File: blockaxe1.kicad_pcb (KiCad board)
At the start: 2 copper layers, 89 parts, among them J1 TC2030-IDC, J3 Conn_01x04, J4 USB_C_Receptacle_USB2.0, J5 Conn_01x02, Q1 2N7002K, U10 DS4432U+, U11 EMC2101, U2 STM32F410CBU6, U5 MCP1824T-1802E, U6 MCP1824T-0802E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

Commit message: migrated over lots of bitaxe parts to blockaxe
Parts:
- added C45: 1uF, Capacitor_SMD:C_0402_1005Metric, F.Cu at (159.9, 132.6)
- added C46: 1uF, Capacitor_SMD:C_0402_1005Metric, F.Cu at (159.9, 134.5)
- added C47: 0.1uF, Capacitor_SMD:C_0402_1005Metric, F.Cu at (162.8, 128.6)
- added C48: 0.1uF, Capacitor_SMD:C_0402_1005Metric, F.Cu at (162.8, 130.6)
- added C49: 1uF, Capacitor_SMD:C_0402_1005Metric, F.Cu at (162.8, 132.6)
- added C50: 1uF, Capacitor_SMD:C_0402_1005Metric, F.Cu at (162.8, 134.5)
- added C51: 330uF, Capacitor_Tantalum_SMD:CP_EIA-7343-31_Kemet-D_Pad2.25x2.55mm_HandSolder, F.Cu at (162.0, 111.8)
- added C7: 0.1uF, Capacitor_SMD:C_0402_1005Metric, F.Cu at (157.1, 128.6)
- added C8: 0.1uF, Capacitor_SMD:C_0402_1005Metric, F.Cu at (157.1, 130.6)
- added J2: TC2030-IDC, blockaxe:Tag-Connect_TC2030-IDC-NL_2x03_P1.27mm_Vertical, F.Cu at (167.3, 79.8)
- added R11: 78.7k 1%, Resistor_SMD:R_0402_1005Metric, F.Cu at (165.1, 118.0)
- added R16: 182k 1%, Resistor_SMD:R_0402_1005Metric, F.Cu at (165.1, 120.0)
- added R17: 130k 1%, Resistor_SMD:R_0402_1005Metric, F.Cu at (165.1, 122.0)
- added R18: 182k 1%, Resistor_SMD:R_0402_1005Metric, F.Cu at (165.1, 124.0)
- added R19: 0, Resistor_SMD:R_0402_1005Metric, F.Cu at (169.1, 118.8)
- added R20: 0, Resistor_SMD:R_0402_1005Metric, F.Cu at (169.1, 120.8)
- added SW1: GT-TC029B-H025-L1N, blockaxe:SW_CS1213AGF260_CRS, F.Cu at (166.5, 70.6)
- added SW2: GT-TC029B-H025-L1N, blockaxe:SW_CS1213AGF260_CRS, F.Cu at (166.5, 75.0)
- added TP15: TestPoint, TestPoint:TestPoint_Pad_D1.0mm, F.Cu at (142.4, 117.8)
- added TP16: TestPoint, TestPoint:TestPoint_Pad_D1.0mm, F.Cu at (142.4, 120.9)
- added TP17: TestPoint, TestPoint:TestPoint_Pad_D1.0mm, F.Cu at (142.4, 124.0)
- added TP19: TestPoint, TestPoint:TestPoint_Pad_D1.0mm, F.Cu at (145.5, 114.8)
- added TP20: TestPoint, TestPoint:TestPoint_Pad_D1.0mm, F.Cu at (145.5, 117.8)
- added TP21: TestPoint, TestPoint:TestPoint_Pad_D1.0mm, F.Cu at (145.5, 120.9)
- added TP22: TestPoint, TestPoint:TestPoint_Pad_D1.0mm, F.Cu at (145.5, 124.0)
- added TP23: TestPoint, TestPoint:TestPoint_Pad_D1.0mm, F.Cu at (148.5, 111.8)
- added TP24: TestPoint, TestPoint:TestPoint_Pad_D1.0mm, F.Cu at (148.5, 114.8)
- added TP25: TestPoint, TestPoint:TestPoint_Pad_D1.0mm, F.Cu at (148.5, 117.8)
- added TP26: TestPoint, TestPoint:TestPoint_Pad_D1.0mm, F.Cu at (148.5, 120.9)
- added U1: ~, blockaxe:bzm2, F.Cu at (155.5, 120.1)
- added U14: 50MHz, blockaxe:OSC_ECS-3225MV-500-CN-TR, F.Cu at (143.9, 127.8)
- added U8: ESP32-S3-WROOM-1, blockaxe:ESP32-S3-WROOM-1, F.Cu at (152.9, 85.0)
- C11: value 0.1uF -> 1uF
- C13: value 1uF -> 0.1uF
- TP1, TP2: footprint TestPoint:TestPoint_Pad_D1.5mm -> TestPoint:TestPoint_Pad_D1.0mm
- U5: value MCP1824T-1802E -> ADP171AUJ-R7; footprint Package_TO_SOT_SMD:SOT-23-5 -> Package_TO_SOT_SMD:TSOT-23-5
- U6: value MCP1824T-0802E -> ADP171AUJ-R7; footprint Package_TO_SOT_SMD:SOT-23-5 -> Package_TO_SOT_SMD:TSOT-23-5
- moved H4 152.5 mm to (238.6, 146.2)
- moved H2 150.2 mm to (238.5, 53.6)
- moved H3 109.2 mm to (189.0, 146.3)
- moved H1 100.4 mm to (189.1, 53.6)
- moved G*** 89.7 mm to (202.8, 174.0)
- moved C12 30.6 mm to (159.9, 128.6)
- moved C13 30.6 mm to (159.9, 130.6)
- moved C10 30.1 mm to (157.1, 132.6)
- moved C11 30.1 mm to (157.1, 134.5)
- moved U6 19.9 mm to (150.5, 134.4)
- moved U5 19.9 mm to (150.5, 130.0)
- moved TP2 8.73 mm to (142.4, 114.8)
- moved TP1 8.30 mm to (142.4, 111.8)
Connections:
- net /Power/VOUT renamed /VDD
- C10 pad 1: /ASIC/5V -> /5V
- C11 pad 1: /ASIC/5V -> /ASIC/1V65
- C12 pad 1: /ASIC/1V8 -> /ASIC/1V2
- C13 pad 1: /ASIC/0V8 -> Net-(C13-Pad1)
- C14 pad 1: /ASIC/3V3 -> /3V3
- C15 pad 1: /ESP32/5V -> /5V
- C17 pad 1: /ESP32/3V3 -> /3V3
- C18 pad 1: /ESP32/3V3 -> /3V3
- C20 pad 1: /ESP32/3V3 -> /3V3
- C22 pad 1: /Power/3V3 -> /3V3
- C23 pad 1: /Power/3V3 -> /3V3
- C24 pad 1: /Fan/5V -> /5V
- C25 pad 1: /Fan/5V -> /5V
- C27 pad 1: /STM32/5V -> /5V
- D1 pad 1: /ESP32/5V -> /5V
- J3 pad 2: /ESP32/3V3 -> /3V3
- J3 pad 3: /ESP32/SCL -> /SCL
- J3 pad 4: /ESP32/SDA -> /SDA
- Q1 pad 1: /Power/PWR_EN -> /PWR_EN
- R3 pad 1: /ESP32/3V3 -> /3V3
- R6 pad 1: /Power/3V3 -> /3V3
- R6 pad 2: /Power/PGOOD -> /PGOOD
- TP1 pad 1: /ASIC/1V8 -> /ASIC/1V2
- TP10 pad 1: /ESP32/3V3 -> /3V3
- TP2 pad 1: /ASIC/0V8 -> /ASIC/1V65
- U10 pad 1: /Power/SDA -> /SDA
- U10 pad 2: /Power/SCL -> /SCL
- U10 pad 8: /Power/3V3 -> /3V3
- U11 pad 7: /Fan/SDA -> /SDA
- U11 pad 8: /Fan/SCL -> /SCL
- U2 pad 17: unconnected-(U2-PA7-Pad17) -> /STM32/RESET
- U2 pad 29: unconnected-(U2-PA8-Pad29) -> /ASIC/TRIP
- U2 pad 30: /STM32/TX1 -> /ESP32/TX
- U2 pad 31: /STM32/RX1 -> /ESP32/RX
- U5 pad 1: /ASIC/5V -> /5V
- U5 pad 3: /ASIC/5V -> /5V
- U5 pad 4: unconnected-(U5-PG-Pad4) -> Net-(U5-ADJ)
- U5 pad 5: /ASIC/1V8 -> /ASIC/1V2
- U6 pad 1: /ASIC/5V -> /5V
- U6 pad 3: /ASIC/5V -> /5V
- U6 pad 4: unconnected-(U6-PG-Pad4) -> Net-(U6-ADJ)
- U6 pad 5: /ASIC/0V8 -> /ASIC/1V65
- U9 pad 10: /Power/3V3 -> /3V3
- U9 pad 8: /Power/SDA -> /SDA
- U9 pad 9: /Power/SCL -> /SCL
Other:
- board outline added: 56.5 x 99.8 mm

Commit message: all the footprints are in?
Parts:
- removed C31, C37: 10uF, Capacitor_SMD:C_0805_2012Metric
- removed C32: 1uF, Capacitor_SMD:C_0805_2012Metric
- removed C33: 3.3nF, Capacitor_SMD:C_0402_1005Metric
- removed C34: 110pF, Capacitor_SMD:C_0402_1005Metric
- removed C35: 4.3nF, Capacitor_SMD:C_0201_0603Metric
- removed C36: 0.1uF, Capacitor_SMD:C_0402_1005Metric
- removed C38: 1.2nF, Capacitor_SMD:C_0805_2012Metric
- removed C39, C40, C41, C42, C43, C44: 100uF, Capacitor_SMD:C_1210_3225Metric
- removed J5: Conn_01x02, Connector_PinHeader_2.54mm:PinHeader_1x02_P2.54mm_Vertical
- removed Q1: 2N7002K, Package_TO_SOT_SMD:SOT-323_SC-70
- removed R10: 2.94k, Resistor_SMD:R_0402_1005Metric
- removed R12: 4.32k, Resistor_SMD:R_0402_1005Metric
- removed R13: 225, Resistor_SMD:R_0402_1005Metric
- removed R14: 10k, Resistor_SMD:R_0402_1005Metric
- removed R15: 60.4k, Resistor_SMD:R_0402_1005Metric
- added C1: 0.1uF, Capacitor_SMD:C_0402_1005Metric, F.Cu at (147.2, 153.5)
- added C2: 4.7uF, Capacitor_SMD:C_0402_1005Metric, F.Cu at (152.7, 155.4)
- added C3: 0.1uF, Capacitor_SMD:C_0402_1005Metric, F.Cu at (147.2, 155.5)
- added C4: 0.1uF, Capacitor_SMD:C_0402_1005Metric, F.Cu at (147.2, 157.4)
- added C5: 0.1uF, Capacitor_SMD:C_0402_1005Metric, F.Cu at (147.2, 159.4)
- added C52: 100uF, Capacitor_SMD:C_1210_3225Metric, F.Cu at (117.5, 153.7)
- added C53: 1uF, Capacitor_SMD:C_0805_2012Metric, F.Cu at (108.3, 153.5)
- added C54: 220nF, Capacitor_SMD:C_0603_1608Metric, F.Cu at (112.5, 159.2)
- added C55: 1uF, Capacitor_SMD:C_0201_0603Metric, F.Cu at (111.7, 161.3)
- added C56: 27nF, Capacitor_SMD:C_0402_1005Metric, F.Cu at (111.9, 153.0)
- added C57: 1nF, Capacitor_SMD:C_0805_2012Metric, F.Cu at (108.3, 156.5)
- added C58: 82pF, Capacitor_SMD:C_0805_2012Metric, F.Cu at (108.3, 159.5)
- added C59: 100pF, Capacitor_SMD:C_0402_1005Metric, F.Cu at (111.9, 154.9)
- added C6: 0.1uF, Capacitor_SMD:C_0402_1005Metric, F.Cu at (147.2, 161.4)
- added C60: 220pF, Capacitor_SMD:C_0805_2012Metric, F.Cu at (108.3, 162.5)
- added C62: 220nF, Capacitor_SMD:C_0402_1005Metric, F.Cu at (111.9, 156.9)
- added D2: XBS104S13R-G, Diode_SMD:D_SOD-323, F.Cu at (124.1, 162.1)
- added J6: Conn_01x04, blockaxe:470531000, F.Cu at (127.4, 169.6)
- added J7: PJ-037AH, blockaxe:CUI_PJ-037AH, F.Cu at (108.8, 171.3)
- added L2: 100nH, blockaxe:FP0805R1-R10-R, F.Cu at (110.4, 147.5)
- added Q4: CSD17575Q3, blockaxe:DQG0008A, F.Cu at (125.2, 158.2)
- added Q5: CSD17312Q5, blockaxe:DQH8, F.Cu at (93.9, 158.3)
- added R1: 10k, Resistor_SMD:R_0402_1005Metric, F.Cu at (150.1, 153.5)
- added R2: 10k, Resistor_SMD:R_0402_1005Metric, F.Cu at (150.1, 155.5)
- added R21: 2.21, Resistor_SMD:R_0402_1005Metric, F.Cu at (121.8, 144.1)
- added R22: 56.2k, Resistor_SMD:R_0402_1005Metric, F.Cu at (121.8, 146.1)
- added R23: 11.8k, Resistor_SMD:R_0402_1005Metric, F.Cu at (121.8, 148.0)
- added R24: 5.23k, Resistor_SMD:R_0402_1005Metric, F.Cu at (121.8, 150.0)
- added R25: 665, Resistor_SMD:R_0402_1005Metric, F.Cu at (121.8, 152.0)
- added R26: 2.67k, Resistor_SMD:R_0402_1005Metric, F.Cu at (124.7, 144.1)
- added R27: 665, Resistor_SMD:R_0402_1005Metric, F.Cu at (124.7, 146.1)
- added R28: 20k, Resistor_SMD:R_0402_1005Metric, F.Cu at (124.7, 148.0)
- added R29: 442, Resistor_SMD:R_0402_1005Metric, F.Cu at (124.7, 150.0)
- added R30: 120k, Resistor_SMD:R_0402_1005Metric, F.Cu at (124.7, 152.0)
- added U12: RT9080-33GJ5, blockaxe:RT9080-33GJ5, F.Cu at (132.2, 145.4)
- added U16: LM27402, blockaxe:SQB16A, F.Cu at (118.7, 158.9)
- added U3: ~, blockaxe:polarity, F.Cu at (94.0, 151.3)
- added U4: TXB0104RGYR, blockaxe:TXB0104, F.Cu at (87.1, 112.5)
- added U7: RT9080-33GJ5, blockaxe:RT9080-33GJ5, F.Cu at (86.3, 122.8)
- added Y1: 32.768kHz, blockaxe:SC32S-7PF20PPM, F.Cu at (86.5, 118.9)
- C29, C30: value 10uF -> 100uF; footprint Capacitor_SMD:C_0805_2012Metric -> Capacitor_SMD:C_1210_3225Metric
- J1: footprint Connector:Tag-Connect_TC2030-IDC-NL_2x03_P1.27mm_Vertical -> blockaxe:Tag-Connect_TC2030-IDC-NL_2x03_P1.27mm_Vertical
- moved C30 41.8 mm to (117.5, 149.4)
- moved C29 40.7 mm to (117.5, 145.2)
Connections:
- C29 pad 1: /5V -> /VDD
- C30 pad 1: /5V -> /VDD
- U10 pad 7: /Power/OUT1 -> unconnected-(U10-OUT1-Pad7)

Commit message: routed the buck reg. started placing board
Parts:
- removed R22: 56.2k, Resistor_SMD:R_0402_1005Metric
- C55: footprint Capacitor_SMD:C_0201_0603Metric -> Capacitor_SMD:C_0603_1608Metric
- J3, J4, J6, U1, U8: moved to B.Cu
- moved J7 158.4 mm to (256.7, 114.5)
- moved C57 145.8 mm to (221.2, 64.2), turned to -90 degrees
- moved C60 145.7 mm to (221.9, 71.3), turned to 180 degrees
- moved C58 145.1 mm to (218.7, 65.5), turned to -90 degrees
- moved H6 144.0 mm to (234.9, 140.7)
- moved Q5 142.6 mm to (211.6, 77.7)
- moved U4 141.2 mm to (228.2, 106.0)
- moved C55 138.5 mm to (209.1, 62.8), turned to 90 degrees
- moved C62 137.9 mm to (222.3, 74.1)
- moved C59 136.1 mm to (220.8, 73.4), turned to -90 degrees
- moved C56 135.6 mm to (216.8, 66.9), turned to -90 degrees
- moved U16 133.2 mm to (213.6, 65.3), turned to 180 degrees
- moved C54 132.7 mm to (207.0, 65.9), turned to 90 degrees
- moved R24 129.0 mm to (220.7, 67.3), turned to -90 degrees
- moved D2 128.1 mm to (209.1, 66.2), turned to 90 degrees
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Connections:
- U16 pad 8: Net-(U16-PGOOD) -> /PGOOD
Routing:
- net Net-(U16-VIN): track 0.00 -> 23.5 mm, vias 0 -> 2
- net Net-(Q5-G): track 0.00 -> 18.3 mm, vias 0 -> 2
- net /VDD: track 0.00 -> 17.4 mm, vias 0 -> 12
- net /Power/OUT0: track 0.00 -> 12.6 mm
- net Net-(Q4-S): track 0.00 -> 11.7 mm, vias 0 -> 2
- net Net-(U16-CS-): track 0.00 -> 10.9 mm
- net Net-(U16-CS+): track 0.00 -> 10.6 mm, vias 0 -> 2
- net GND: track 0.00 -> 9.67 mm, vias 0 -> 18
- net Net-(D2-K): track 0.00 -> 9.03 mm
- net Net-(U16-COMP): track 0.00 -> 6.42 mm
- net Net-(Q4-G): track 0.00 -> 4.49 mm
- net Net-(D2-A): track 0.00 -> 4.26 mm
- net Net-(C62-Pad1): track 0.00 -> 2.57 mm
- net Net-(C57-Pad2): track 0.00 -> 1.80 mm
- net Net-(C60-Pad2): track 0.00 -> 1.57 mm
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- added copper zone on F.Cu, net /5V
- added copper zone on B.Cu, net /VDD
- added copper zone on F.Cu, net /VDD
- added copper zone on B.Cu, net GND
- added copper zone on F.Cu, net GND
- added copper zone on In1.Cu, net GND
- added copper zone on F.Cu, net Net-(Q4-S)
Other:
- copper layers 2 -> 4

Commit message: more placing and routing
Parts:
- removed J7: PJ-037AH, blockaxe:CUI_PJ-037AH
- added J5: 54-00164, blockaxe:BarrelJack_Wuerth_694106106102_2.0x5.5mm, B.Cu at (111.6, 64.7)
- C24, SW1, SW2, U3: moved to B.Cu
- J3: footprint Connector_PinHeader_2.54mm:PinHeader_1x04_P2.54mm_Vertical -> Connector_PinSocket_2.54mm:PinSocket_1x04_P2.54mm_Vertical_SMD_Pin1Right
- moved J4 132.7 mm to (107.1, 85.6), turned to 90 degrees
- moved C47 117.8 mm to (45.3, 120.7)
- moved C48 117.8 mm to (45.3, 122.6)
- moved C49 117.8 mm to (45.3, 124.6)
- moved C50 117.8 mm to (45.3, 126.6)
- moved C13 117.8 mm to (42.4, 122.6)
- moved C45 117.8 mm to (42.4, 124.6)
- moved C46 117.8 mm to (42.4, 126.6)
- moved R19 117.8 mm to (51.5, 110.9)
- moved R20 117.8 mm to (51.5, 112.9)
- moved TP23 117.8 mm to (31.0, 103.8)
- moved TP24 117.8 mm to (31.0, 106.8)
- moved TP25 117.8 mm to (31.0, 109.9)
- moved TP26 117.8 mm to (31.0, 112.9)
- moved TP1 117.8 mm to (24.9, 103.8)
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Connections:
- net Net-(Q4-S) renamed /Power/SW
- C10 pad 1: /5V -> /3V3
- C13 pad 1: Net-(C13-Pad1) -> Net-(U1-VDD_INT_1)
- C8 pad 1: /5V -> /3V3
- U1 pad 1: Net-(C13-Pad1) -> Net-(U1-VDD_INT_1)
- U1 pad 12: Net-(C13-Pad1) -> unconnected-(U1-VDD_INT_2-Pad12)
- U1 pad 58: /ASIC/1V2 -> GND
- U5 pad 1: /5V -> /3V3
- U5 pad 3: /5V -> /3V3
- U6 pad 1: /5V -> /3V3
- U6 pad 3: /5V -> /3V3
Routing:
- net /ESP32/RX: track 0.00 -> 31.9 mm, vias 0 -> 1
- net /ESP32/TX: track 0.00 -> 31.8 mm, vias 0 -> 1
- net Net-(U8-GPIO20/U1CTS/ADC2_CH9/CLK_OUT1/USB_D+): track 0.00 -> 31.2 mm
- net Net-(U8-GPIO19/U1RTS/ADC2_CH8/CLK_OUT2/USB_D-): track 0.00 -> 30.7 mm
- net GND: track 9.67 -> 39.5 mm, vias 18 -> 34
- net /3V3: track 0.00 -> 15.8 mm, vias 0 -> 6
- net /Power/OUT0: track 12.6 -> 22.7 mm
- net /5V: track 0.00 -> 9.02 mm
- net /ASIC/1V65: track 0.00 -> 6.90 mm
- net /Power/VIN: track 0.00 -> 6.53 mm, vias 0 -> 7
- net /ASIC/CLK: track 0.00 -> 6.45 mm, vias 0 -> 1
- net Net-(U16-VIN): track 23.5 -> 18.3 mm
- net Net-(J4-CC1): track 0.00 -> 5.16 mm, vias 0 -> 1
- net /ESP32/XIN32: track 0.00 -> 4.16 mm, vias 0 -> 1
- net /ESP32/XOUT32: track 0.00 -> 3.98 mm, vias 0 -> 1
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- added copper zone on In2.Cu, net /3V3
- added copper zone on B.Cu, net /Power/VIN
- added copper zone on F.Cu, net /Power/VIN
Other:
- board text added: "BOOT"
- board text added: "RESET"

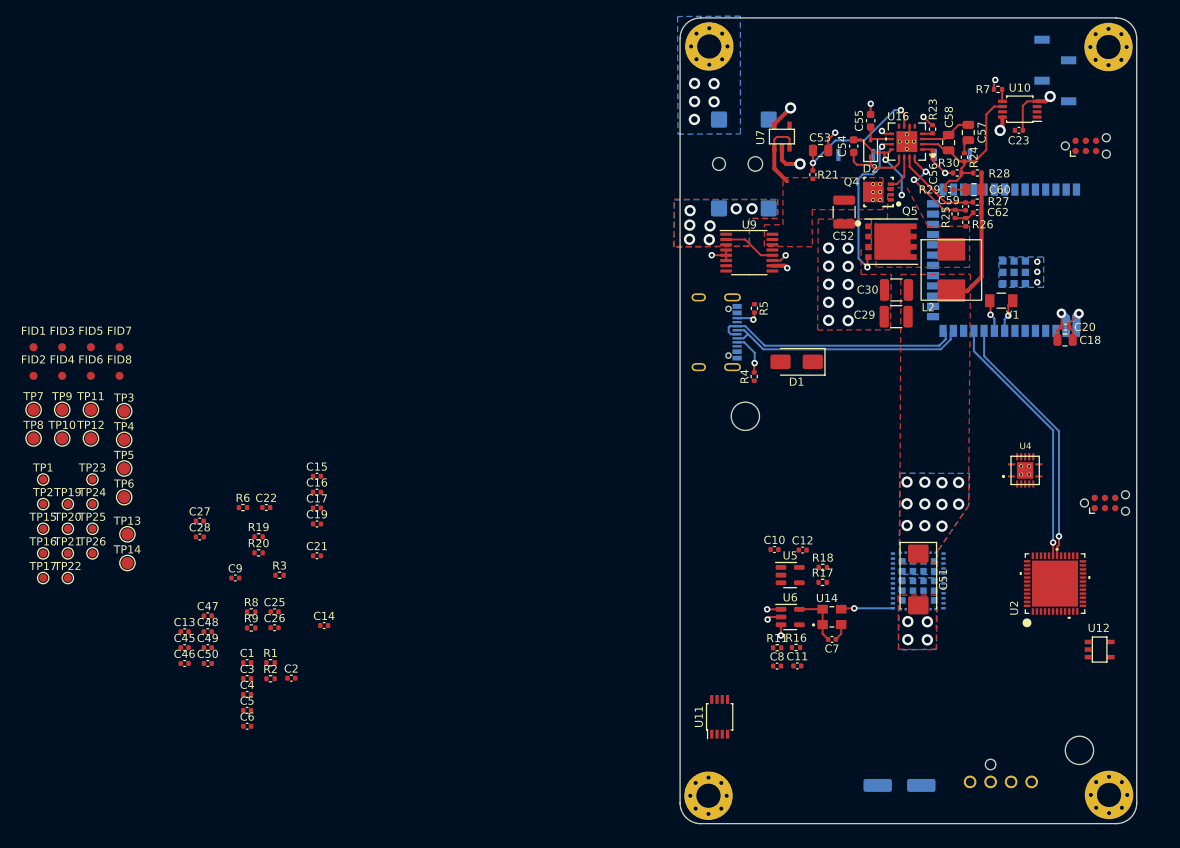
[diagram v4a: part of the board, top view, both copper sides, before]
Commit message: more routing. switched to RA buttons, moved the buck closer to the barrel
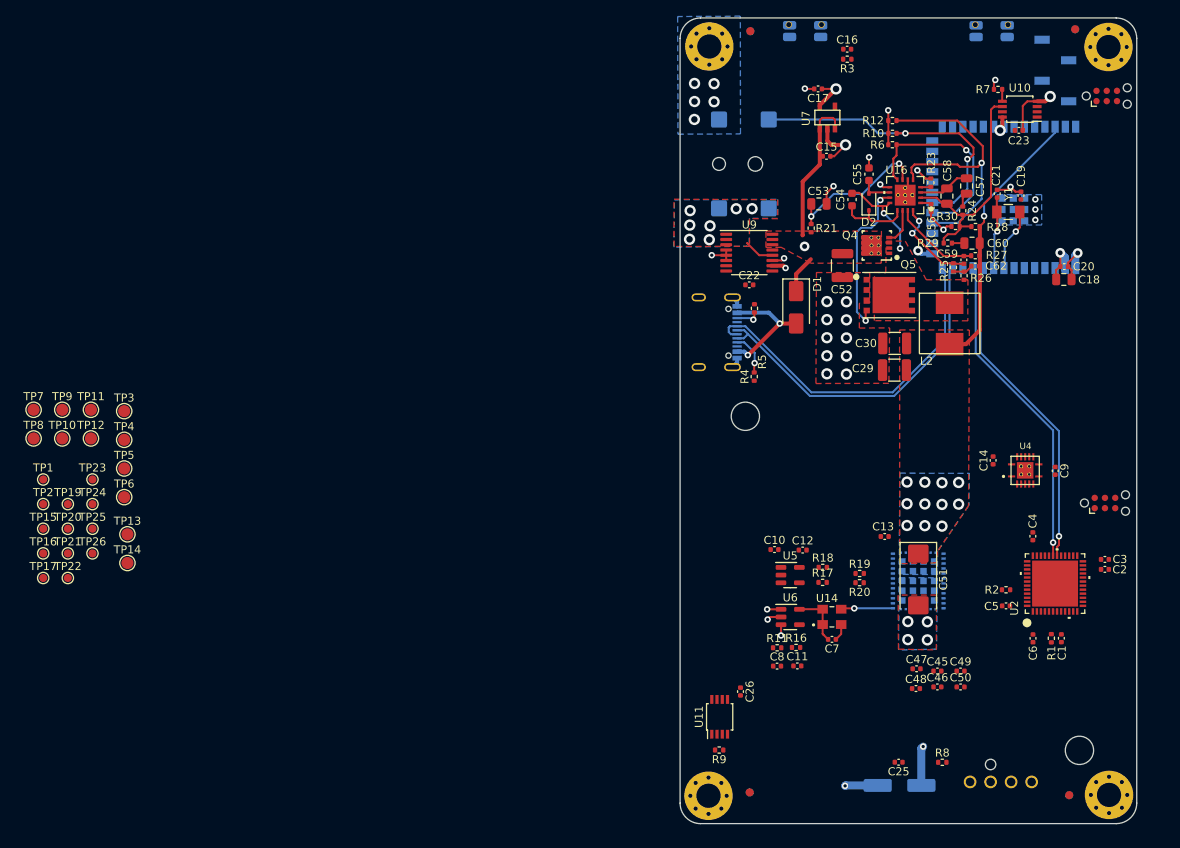
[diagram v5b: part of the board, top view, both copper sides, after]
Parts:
- removed C27, C28: 1uF, Capacitor_SMD:C_0402_1005Metric
- removed U12: RT9080-33GJ5, blockaxe:RT9080-33GJ5
- added R10: 1M, Resistor_SMD:R_0402_1005Metric, F.Cu at (130.0, 60.9)
- added R12: 10k, Resistor_SMD:R_0402_1005Metric, F.Cu at (130.0, 59.4)
- FID2, FID3, FID5, FID6: moved to B.Cu
- SW1, SW2: value GT-TC029B-H025-L1N -> EVQ-9P701P; footprint blockaxe:SW_CS1213AGF260_CRS -> blockaxe:EVQ9P701P-switch
- moved FID2 138.4 mm to (151.9, 142.9), turned to 180 degrees
- moved FID4 135.1 mm to (151.9, 142.9)
- moved FID5 128.1 mm to (152.7, 48.0), turned to 180 degrees
- moved FID7 124.7 mm to (152.7, 48.0)
- moved C3 107.2 mm to (156.3, 113.7)
- moved C9 102.4 mm to (150.2, 102.7), turned to -90 degrees
- moved C2 101.6 mm to (156.3, 114.9)
- moved C1 100.9 mm to (150.9, 123.5), turned to -90 degrees
- moved C4 99.2 mm to (147.4, 110.8), turned to 90 degrees
- moved C6 97.9 mm to (147.4, 123.5), turned to -90 degrees
- moved FID1 97.0 mm to (112.4, 48.3)
- moved R1 96.7 mm to (149.7, 123.5), turned to -90 degrees
- moved FID6 96.5 mm to (112.4, 142.5), turned to 180 degrees
- moved C19 96.2 mm to (145.9, 68.6), turned to 90 degrees
- moved C21 95.4 mm to (143.0, 68.4), turned to 90 degrees
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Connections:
- C10 pad 1: /3V3 -> VDD
- C14 pad 1: /3V3 -> VDD
- C17 pad 1: /3V3 -> VDD
- C18 pad 1: /3V3 -> VDD
- C20 pad 1: /3V3 -> VDD
- C22 pad 1: /3V3 -> VDD
- C23 pad 1: /3V3 -> VDD
- C8 pad 1: /3V3 -> VDD
- J2 pad 2: /3V3 -> VDD
- J3 pad 2: /3V3 -> VDD
- R3 pad 1: /3V3 -> VDD
- R6 pad 1: /3V3 -> VDD
- TP10 pad 1: /3V3 -> VDD
- U10 pad 8: /3V3 -> VDD
- U4 pad 14: /3V3 -> VDD
- U5 pad 1: /3V3 -> VDD
- U5 pad 3: /3V3 -> VDD
- U6 pad 1: /3V3 -> VDD
- U6 pad 3: /3V3 -> VDD
- U7 pad 5: /3V3 -> VDD
- U8 pad 15: /3V3 -> VDD
- U8 pad 2: /3V3 -> VDD
- U8 pad 20: unconnected-(U8-GPIO12/TOUCH12/ADC2_CH1/FSPICLK/FSPIIO6/SUBSPICLK-Pad20) -> /PLUG_SENSE
- U9 pad 10: /3V3 -> VDD
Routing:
- net /5V: track 9.02 -> 132.0 mm, vias 0 -> 2
- net /PLUG_SENSE: track 0.00 -> 38.5 mm, vias 0 -> 2
- net /PWR_EN: track 0.00 -> 36.7 mm, vias 0 -> 1
- net /PGOOD: track 0.00 -> 25.5 mm, vias 0 -> 1
- net VDD: track 0.00 -> 21.9 mm, vias 0 -> 8
- net /VDD: track 17.4 -> 33.7 mm, vias 11 -> 12
- net /3V3: track 15.8 -> 0.00 mm, vias 6 -> 0
- net Net-(D1-Pad2): track 0.00 -> 15.0 mm, vias 0 -> 2
- net GND: track 39.5 -> 54.2 mm, vias 34 -> 37
- net Net-(U8-GPIO20/U1CTS/ADC2_CH9/CLK_OUT1/USB_D+): track 31.2 -> 43.7 mm
- net Net-(U8-GPIO19/U1RTS/ADC2_CH8/CLK_OUT2/USB_D-): track 30.7 -> 43.2 mm
- net /ESP32/TX: track 31.8 -> 39.9 mm
- net /ESP32/RX: track 31.9 -> 39.7 mm
- net /Power/OUT0: track 22.7 -> 29.4 mm
- net /ESP32/XOUT32: track 3.98 -> 8.99 mm
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- added copper zone on In2.Cu, net VDD
- removed copper zone on In2.Cu, net /3V3
